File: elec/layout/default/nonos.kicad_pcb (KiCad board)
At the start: 2 copper layers, 59 parts, among them CN1 HRSHirose_DF40C_100DS_0_4V51, CN2 HRSHirose_DF40C_100DS_0_4V51, Q1 MOSFET, U1 STUSB4500QTR, U2 _Texas_Instruments_SN74LVC1G0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, U3 _Texas_Instruments_TAS5825MRH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, U4 Texas_Instruments_TPS56637RPAR

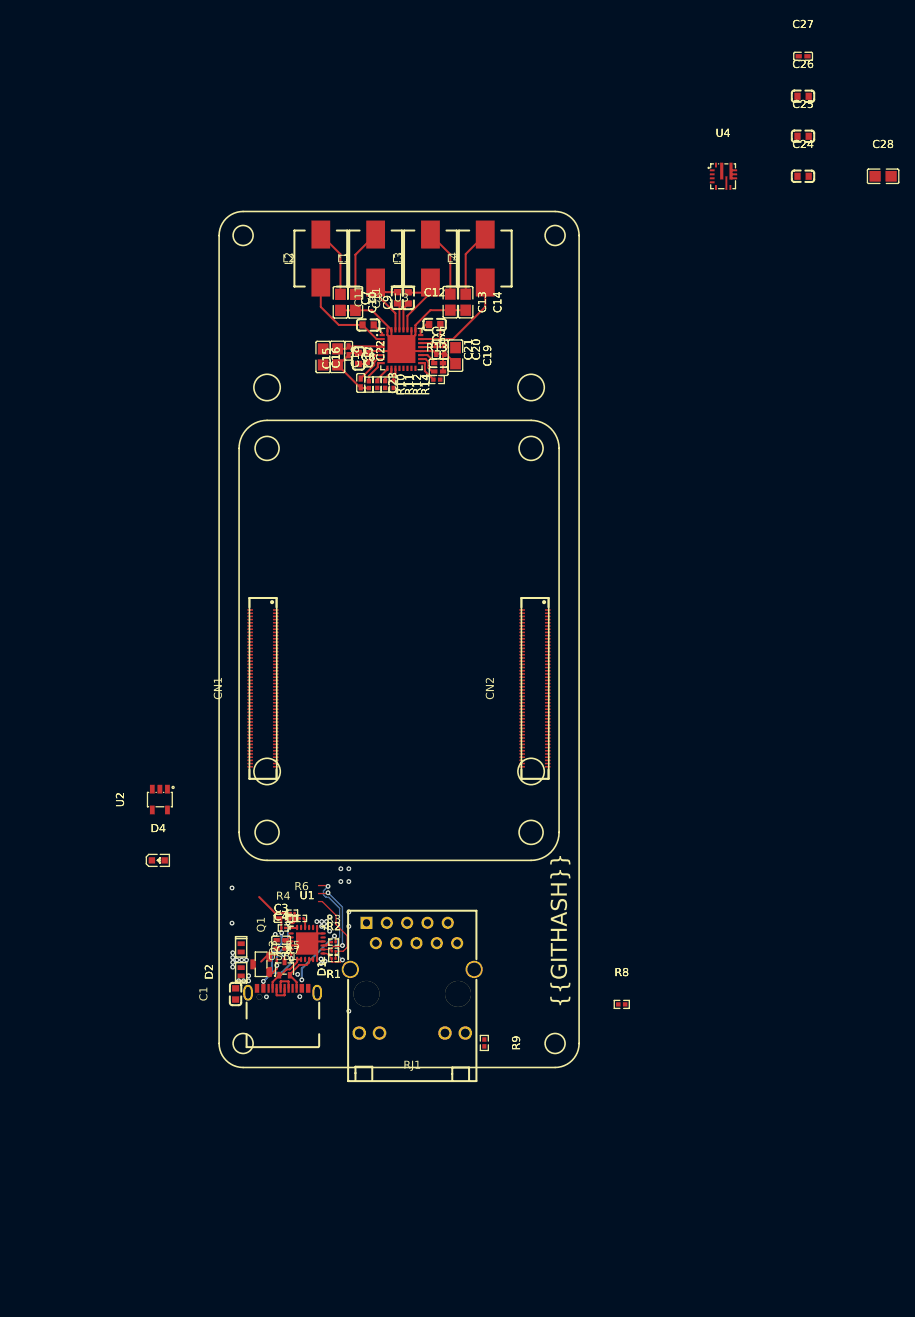
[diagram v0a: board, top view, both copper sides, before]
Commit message: import copper features to hat board
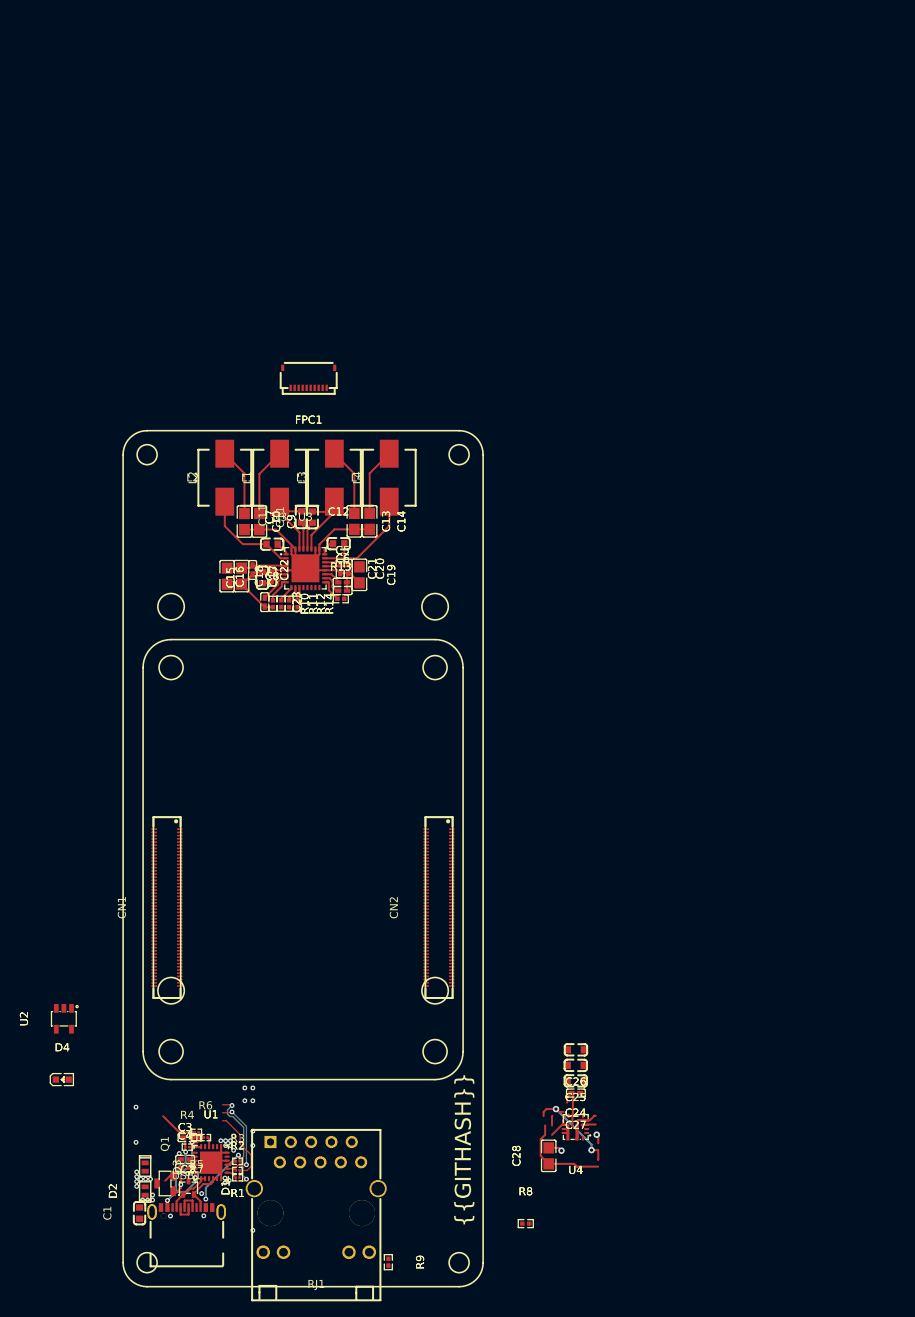
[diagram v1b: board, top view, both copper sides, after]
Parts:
- added FPC1: TE_Connectivity_1_2328702_0, lcsc:FPC-SMD_10P-P0.50_HDGC_0.5K-HX-10PWB, F.Cu at (139.8, 52.8)
- C5: value 1µF ±10% 25V X5R -> (none)
- C6: value (none) -> 1µF ±10% 25V X5R
- L1: value (none) -> 10µH ±20% 4.5A 68mΩ
- L2: value 10µH ±20% 4.5A 68mΩ -> (none)
- R1: value (none) -> 1kΩ ±1% 50mW
- R4: value 1kΩ ±1% 50mW -> (none)
- moved C27 132.7 mm to (173.2, 142.2), turned to 180 degrees
- moved C28 129.4 mm to (169.8, 150.0), turned to 90 degrees
- moved C26 122.5 mm to (173.2, 136.8), turned to 180 degrees
- moved U4 120.3 mm to (173.2, 146.4), turned to 180 degrees
- moved C25 119.6 mm to (173.2, 138.7), turned to 180 degrees
- moved C24 116.6 mm to (173.2, 140.7), turned to 180 degrees
- moved R4 29.9 mm to (124.6, 149.0)
- moved Q1 29.9 mm to (121.9, 153.5)
- moved R7 29.9 mm to (125.8, 147.8)
- moved C1 29.9 mm to (118.7, 157.2)
- moved C10 29.9 mm to (131.8, 70.8)
- moved C17 29.9 mm to (131.4, 77.6)
- moved C18 29.9 mm to (129.6, 77.6)
- moved C20 29.9 mm to (144.8, 76.7)
- moved C21 29.9 mm to (143.8, 76.7)
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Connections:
- net pins[39] renamed processor.hdi_b-pins[39]
- net pins[49] renamed processor.hdi_b-pins[49]
- net processor-pins[44] renamed pins[44]
- net processor.hdi_b-pins[23] renamed pins[23]
- net processor.hdi_b-pins[27] renamed pins[27]
- net processor.hdi_b-pins[29] renamed pins[29]
- net processor.hdi_b-pins[40] renamed pins[40]
- C1 pad 1: pd_controller-lv -> lv-1
- C10 pad 1: amplifier-signal -> amplifier-signal-2
- C11 pad 1: amplifier-net-9 -> amplifier-net-8
- C11 pad 2: amplifier-net-10 -> amplifier-net-5
- C12 pad 1: amplifier-net-7 -> amplifier-net-12
- C12 pad 2: amplifier-net-8 -> amplifier-net-11
- C13 pad 1: amplifier-signal-2 -> amplifier-signal
- C2 pad 1: pd_controller-net-1 -> pd_controller-net-4
- C23 pad 1: amplifier-net-14 -> amplifier-net-3
- C24 pad 1: regulator-net -> VSINK_VCC
- C24 pad 2: regulator-net-1 -> lv-1
- C25 pad 1: regulator-net -> VSINK_VCC
- C25 pad 2: regulator-net-1 -> lv-1
- C26 pad 1: regulator-net -> VSINK_VCC
- C26 pad 2: regulator-net-1 -> lv-1
- C27 pad 1: regulator-net -> VSINK_VCC
- C27 pad 2: regulator-net-1 -> lv-1
- C28 pad 1: regulator-hv -> hv
- C28 pad 2: regulator-net-1 -> lv-1
- C3 pad 1: pd_controller-lv -> lv-1
- C4 pad 1: pd_controller-lv -> lv-1
- C5 pad 1: amplifier-net-13 -> amplifier-net-4
- C6 pad 1: amplifier-net-5 -> amplifier-net-10
- C7 pad 1: amplifier-net-15 -> amplifier-net
- C7 pad 2: amplifier-net-6 -> amplifier-net-1
- C8 pad 1: amplifier-net-16 -> amplifier-net-7
- C8 pad 2: amplifier-net-1 -> amplifier-net-6
- CN1 pad 12: processor-pins[23] -> processor-signal-1
- CN1 pad 14: processor-pins[27] -> processor-signal-4
- CN1 pad 15: processor-pins[29] -> signal-1
- CN1 pad 17: processor-signal-4 -> signal-2
- CN1 pad 19: processor-signal-7 -> processor-signal
- CN1 pad 20: processor-signal-3 -> processor-pins[39]
- CN1 pad 23: pins[45] -> processor-signal-6
- CN1 pad 24: pins[47] -> processor-signal-5
- CN1 pad 25: processor-signal-6 -> processor-pins[49]
- CN1 pad 27: pins[53] -> signal
- CN1 pad 28: processor-signal-2 -> signal-5
- CN1 pad 29: processor-signal -> signal-6
- CN1 pad 73: pins[54] -> processor-signal-3
- CN1 pad 78: processor-pins[44]-1 -> processor-signal-7
- CN1 pad 80: processor-pins[40] -> processor-signal-2
- CN1 pad 82: processor-signal-5 -> signal-3
- CN1 pad 85: processor-signal-1 -> pins[30]
- D1 pad 3: pd_controller-lv -> lv-1
- D2 pad 2: pd_controller-lv -> lv-1
- D3 pad 2: pd_controller-lv -> lv-1
- L1 pad 1: amplifier-net-6 -> amplifier-net-1
- L2 pad 1: amplifier-net-1 -> amplifier-net-6
- L2 pad 2: amplifier-signal -> amplifier-signal-2
- L3 pad 1: amplifier-net-10 -> amplifier-net-5
- L3 pad 2: amplifier-signal-2 -> amplifier-signal
- L4 pad 1: amplifier-net-8 -> amplifier-net-11
- R1 pad 2: pd_controller-net-2 -> pd_controller-net-3
- R10 pad 1: amplifier-net-4 -> amplifier-net-9
- R11 pad 1: amplifier-net-11 -> signal-6
- R11 pad 2: amplifier.fault-hv -> VCC_3V3
- R12 pad 1: amplifier-net -> signal-7
- R12 pad 2: amplifier.mute-hv -> VCC_3V3
- R13 pad 1: amplifier-net-12 -> signal-5
- R13 pad 2: amplifier.pdn-hv -> VCC_3V3
- R14 pad 1: amplifier-net-3 -> signal-4
- R14 pad 2: amplifier.warn-hv -> VCC_3V3
- R4 pad 2: pd_controller-net-3 -> pd_controller-net-2
- R6 pad 2: pd_controller-net-4 -> pd_controller-net-1
- R7 pad 2: pd_controller-net-1 -> pd_controller-net-4
- U1 pad 10: pd_controller-lv -> lv-1
- U1 pad 12: pd_controller-lv -> lv-1
- U1 pad 13: pd_controller-lv -> lv-1
- U1 pad 16: pd_controller-net-4 -> pd_controller-net-1
- U1 pad 18: pd_controller-net-3 -> pd_controller-net-2
- U1 pad 22: pd_controller-lv -> lv-1
- U1 pad 25: pd_controller-lv -> lv-1
- U1 pad 6: pd_controller-lv -> lv-1
- U1 pad 9: pd_controller-net-2 -> pd_controller-net-3
- U3 pad 1: amplifier-net-16 -> amplifier-net-7
- U3 pad 10: amplifier-net -> signal-7
- U3 pad 11: amplifier-net-3 -> signal-4
- U3 pad 12: lrclk -> I2S_WS
- U3 pad 13: sclk -> I2S_SCK
- U3 pad 14: sdin -> I2S_SD
- U3 pad 15: sda -> SDA
- U3 pad 16: scl -> SCL
- U3 pad 17: amplifier-net-12 -> signal-5
- U3 pad 18: amplifier-net-5 -> amplifier-net-10
- U3 pad 19: amplifier-net-13 -> amplifier-net-4
- U3 pad 2: amplifier-net-1 -> amplifier-net-6
- U3 pad 23: amplifier-net-8 -> amplifier-net-11
- U3 pad 24: amplifier-net-7 -> amplifier-net-12
- U3 pad 27: amplifier-net-10 -> amplifier-net-5
- U3 pad 28: amplifier-net-9 -> amplifier-net-8
- U3 pad 29: amplifier-net-15 -> amplifier-net
- U3 pad 30: amplifier-net-6 -> amplifier-net-1
- U3 pad 7: amplifier-net-14 -> amplifier-net-3
- U3 pad 8: amplifier-net-4 -> amplifier-net-9
- U3 pad 9: amplifier-net-11 -> signal-6
- USB1 pad 1: pd_controller-lv -> lv-1
- USB1 pad 12: pd_controller-lv -> lv-1
- USB1 pad 13: pd_controller-lv -> lv-1
- USB1 pad 14: pd_controller-lv -> lv-1
- USB1 pad 5: pd_controller.USB_CONNECTOR-net -> pd_controller.USB_CONNECTOR-net-1
- USB1 pad 6: pd_controller.USB_CONNECTOR-net-1 -> pd_controller.USB_CONNECTOR-net
- USB1 pad 7: pd_controller.USB_CONNECTOR-net -> pd_controller.USB_CONNECTOR-net-1
- USB1 pad 8: pd_controller.USB_CONNECTOR-net-1 -> pd_controller.USB_CONNECTOR-net
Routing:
- net lv-1: track 0.00 -> 20.0 mm, vias 0 -> 2
- net pd_controller-lv: track 12.7 -> 0.00 mm, vias 29 -> 0
- net amplifier-net-11: track 2.11 -> 14.6 mm
- net I2S_WS: track 0.00 -> 12.3 mm, vias 0 -> 2
- net hv: track 0.00 -> 11.8 mm
- net amplifier-net-8: track 14.6 -> 3.53 mm
- net amplifier-net-10: track 10.8 -> 2.78 mm
- net amplifier-net-5: track 2.78 -> 10.8 mm
- net processor.hdi_a-pins[56]: track 0.00 -> 4.99 mm
- net amplifier-net-14: track 4.03 -> 0.00 mm
- net amplifier-net-15: track 3.41 -> 0.00 mm
- net signal-5: track 0.00 -> 3.34 mm
- net vin: track 0.00 -> 2.46 mm
- net amplifier-net-3: track 1.70 -> 4.03 mm
- net amplifier-net-1: track 12.4 -> 10.2 mm
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
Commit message: add capacitive sensor IC and cleanup
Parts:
- C5: value (none) -> 1µF ±10% 25V X5R
- C6: value 1µF ±10% 25V X5R -> (none)
- L1: value 10µH ±20% 4.5A 68mΩ -> (none)
- L2: value (none) -> 10µH ±20% 4.5A 68mΩ
- R1: value 1kΩ ±1% 50mW -> (none)
- R4: value (none) -> 1kΩ ±1% 50mW
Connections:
- net pins[23] renamed processor.hdi_b-pins[23]
- net pins[40] renamed processor.hdi_b-pins[40]
- net processor-pins[38] renamed processor-signal-8
- net processor-pins[46] renamed pins[46]
- net processor.hdi_b-pins[26] renamed pins[26]
- net processor.hdi_b-pins[38] renamed pins[38]
- net processor.hdi_b-pins[39] renamed pins[39]
- net processor.hdi_b-pins[49] renamed pins[49]
- C1 pad 1: lv-1 -> lv
- C10 pad 1: amplifier-signal-2 -> amplifier-signal-1
- C10 pad 2: amplifier-net-2 -> amplifier-net
- C11 pad 1: amplifier-net-8 -> amplifier-net-12
- C11 pad 2: amplifier-net-5 -> amplifier-net-9
- C12 pad 1: amplifier-net-12 -> amplifier-net-10
- C12 pad 2: amplifier-net-11 -> amplifier-net-4
- C13 pad 1: amplifier-signal -> amplifier-signal-3
- C13 pad 2: amplifier-net-2 -> amplifier-net
- C14 pad 1: amplifier-signal-3 -> amplifier-signal
- C14 pad 2: amplifier-net-2 -> amplifier-net
- C15 pad 2: amplifier-net-2 -> amplifier-net
- C16 pad 2: amplifier-net-2 -> amplifier-net
- C17 pad 2: amplifier-net-2 -> amplifier-net
- C18 pad 2: amplifier-net-2 -> amplifier-net
- C19 pad 2: amplifier-net-2 -> amplifier-net
- C2 pad 1: pd_controller-net-4 -> pd_controller-net
- C20 pad 2: amplifier-net-2 -> amplifier-net
- C21 pad 2: amplifier-net-2 -> amplifier-net
- C22 pad 2: amplifier-net-2 -> amplifier-net
- C23 pad 1: amplifier-net-3 -> amplifier-net-6
- C23 pad 2: amplifier-net-2 -> amplifier-net
- C24 pad 2: lv-1 -> lv
- C25 pad 2: lv-1 -> lv
- C26 pad 2: lv-1 -> lv
- C27 pad 2: lv-1 -> lv
- C28 pad 2: lv-1 -> lv
- C3 pad 1: lv-1 -> lv
- C4 pad 1: lv-1 -> lv
- C5 pad 1: amplifier-net-4 -> amplifier-net-7
- C5 pad 2: amplifier-net-2 -> amplifier-net
- C6 pad 1: amplifier-net-10 -> amplifier-net-3
- C6 pad 2: amplifier-net-2 -> amplifier-net
- C7 pad 1: amplifier-net -> amplifier-net-11
- C7 pad 2: amplifier-net-1 -> amplifier-net-5
- C8 pad 1: amplifier-net-7 -> amplifier-net-8
- C8 pad 2: amplifier-net-6 -> amplifier-net-1
- C9 pad 1: amplifier-signal-1 -> amplifier-signal-2
- C9 pad 2: amplifier-net-2 -> amplifier-net
- CN1 pad 12: processor-signal-1 -> processor-pins[23]
- CN1 pad 14: processor-signal-4 -> processor-signal-7
- CN1 pad 15: signal-1 -> signal-3
- CN1 pad 17: signal-2 -> signal-5
- CN1 pad 19: processor-signal -> pins[37]
- CN1 pad 20: processor-pins[39] -> processor-signal-6
- CN1 pad 23: processor-signal-6 -> pins[45]
- CN1 pad 24: processor-signal-5 -> pins[47]
- CN1 pad 25: processor-pins[49] -> processor-signal-2
- CN1 pad 27: signal -> signal-2
- CN1 pad 28: signal-5 -> signal-6
- CN1 pad 29: signal-6 -> signal-1
- CN1 pad 73: processor-signal-3 -> processor-signal-1
- CN1 pad 77: processor-pins[46]-1 -> processor-signal-5
- CN1 pad 78: processor-signal-7 -> processor-signal-4
- CN1 pad 80: processor-signal-2 -> processor-pins[40]
- CN1 pad 82: signal-3 -> signal-4
- CN1 pad 85: pins[30] -> processor-signal-3
- CN1 pad 87: processor-pins[26] -> processor-signal
- D1 pad 3: lv-1 -> lv
- D2 pad 2: lv-1 -> lv
- D3 pad 2: lv-1 -> lv
- FPC1 pad 10: signal-3 -> signal-4
- FPC1 pad 3: lv-1 -> lv
- FPC1 pad 6: lv -> lv-1
- FPC1 pad 7: signal -> signal-2
- FPC1 pad 8: signal-2 -> signal-5
- FPC1 pad 9: signal-1 -> signal-3
- L1 pad 1: amplifier-net-1 -> amplifier-net-5
- L1 pad 2: amplifier-signal-1 -> amplifier-signal-2
- L2 pad 1: amplifier-net-6 -> amplifier-net-1
- L2 pad 2: amplifier-signal-2 -> amplifier-signal-1
- L3 pad 1: amplifier-net-5 -> amplifier-net-9
- L3 pad 2: amplifier-signal -> amplifier-signal-3
- L4 pad 1: amplifier-net-11 -> amplifier-net-4
- L4 pad 2: amplifier-signal-3 -> amplifier-signal
- Q1 pad 1: pd_controller-net -> pd_controller-net-1
- R1 pad 2: pd_controller-net-3 -> pd_controller-net-4
- R10 pad 1: amplifier-net-9 -> amplifier-net-2
- R10 pad 2: amplifier-net-2 -> amplifier-net
- R11 pad 1: signal-6 -> signal-1
- R13 pad 1: signal-5 -> signal-6
- R14 pad 1: signal-4 -> signal
- R4 pad 2: pd_controller-net-2 -> pd_controller-net-3
- R5 pad 1: pd_controller-net -> pd_controller-net-1
- R6 pad 1: pd_controller-net -> pd_controller-net-1
- R6 pad 2: pd_controller-net-1 -> pd_controller-net-2
- R7 pad 1: pd_controller-net -> pd_controller-net-1
- R7 pad 2: pd_controller-net-4 -> pd_controller-net
- RJ1 pad SHIELD0: lv -> lv-1
- RJ1 pad SHIELD1: lv -> lv-1
- U1 pad 10: lv-1 -> lv
- U1 pad 12: lv-1 -> lv
- U1 pad 13: lv-1 -> lv
- U1 pad 16: pd_controller-net-1 -> pd_controller-net-2
- U1 pad 18: pd_controller-net-2 -> pd_controller-net-3
- U1 pad 22: lv-1 -> lv
- U1 pad 25: lv-1 -> lv
- U1 pad 6: lv-1 -> lv
- U1 pad 9: pd_controller-net-3 -> pd_controller-net-4
- U3 pad 1: amplifier-net-7 -> amplifier-net-8
- U3 pad 11: signal-4 -> signal
- U3 pad 17: signal-5 -> signal-6
- U3 pad 18: amplifier-net-10 -> amplifier-net-3
- U3 pad 19: amplifier-net-4 -> amplifier-net-7
- U3 pad 2: amplifier-net-6 -> amplifier-net-1
- U3 pad 20: amplifier-net-2 -> amplifier-net
- U3 pad 23: amplifier-net-11 -> amplifier-net-4
- U3 pad 24: amplifier-net-12 -> amplifier-net-10
- U3 pad 25: amplifier-net-2 -> amplifier-net
- U3 pad 26: amplifier-net-2 -> amplifier-net
- U3 pad 27: amplifier-net-5 -> amplifier-net-9
- U3 pad 28: amplifier-net-8 -> amplifier-net-12
- U3 pad 29: amplifier-net -> amplifier-net-11
- U3 pad 30: amplifier-net-1 -> amplifier-net-5
- U3 pad 31: amplifier-net-2 -> amplifier-net
- U3 pad 32: amplifier-net-2 -> amplifier-net
- U3 pad 33: amplifier-net-2 -> amplifier-net
- U3 pad 5: amplifier-net-2 -> amplifier-net
- U3 pad 7: amplifier-net-3 -> amplifier-net-6
- U3 pad 8: amplifier-net-9 -> amplifier-net-2
- U3 pad 9: signal-6 -> signal-1
- USB1 pad 1: lv-1 -> lv
- USB1 pad 12: lv-1 -> lv
- USB1 pad 13: lv-1 -> lv
- USB1 pad 14: lv-1 -> lv
